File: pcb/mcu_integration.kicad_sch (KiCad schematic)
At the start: 28 parts, among them J1 Micro_SD_Card, U1 STM32F103RBTx, Y1 ECS-80-18-5PX-GM-TR

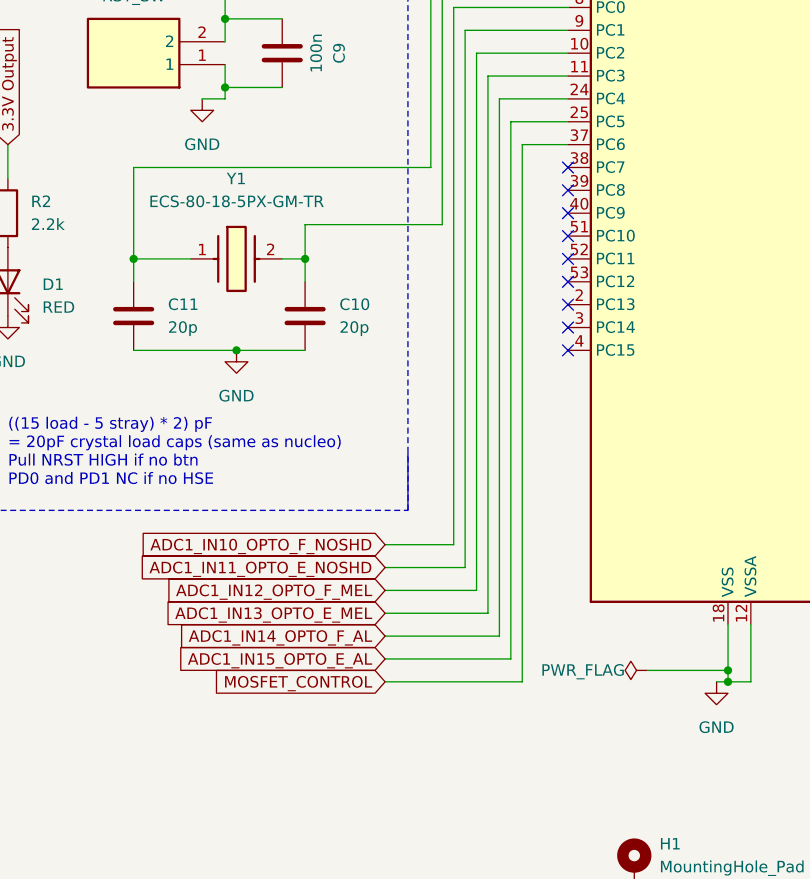
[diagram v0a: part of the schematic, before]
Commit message: mcu square wave sine header, more space for ic's should be ready for order
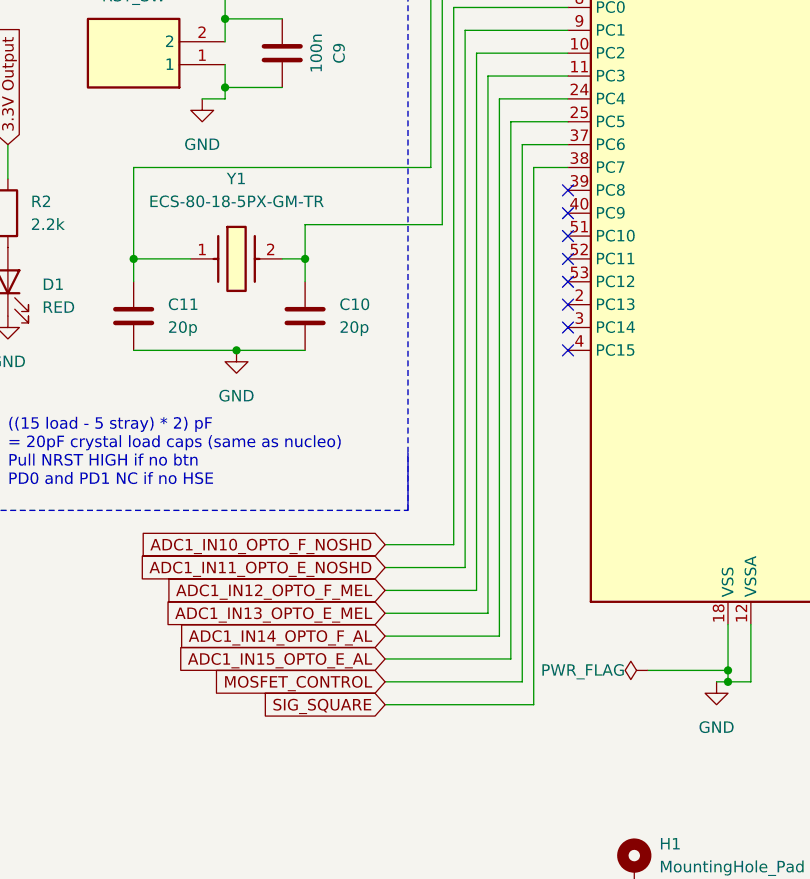
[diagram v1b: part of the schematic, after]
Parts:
- C1: footprint Capacitor_SMD:C_0402_1005Metric -> Resistor_SMD:R_0402_1005Metric
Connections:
- net SIG_SQUARE: now reaches U1.38 (PC7)
- no-connect marks 27 -> 26
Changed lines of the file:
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@@
   (no_connect (at 116.84 107.95))
   (no_connect (at 81.28 85.09))
-  (no_connect (at 81.28 74.93))
   (no_connect (at 81.28 80.01))
   (no_connect (at 116.84 90.17))
@@
     (stroke (width 0) (type default))
   )
+  (wire (pts (xy 60.96 134.62) (xy 77.47 134.62))
+    (stroke (width 0) (type default))
+  )
   (polyline (pts (xy 13.97 113.03) (xy 63.5 113.03))
     (stroke (width 0) (type dash))
@@
     (stroke (width 0) (type default))
   )
+  (wire (pts (xy 77.47 134.62) (xy 77.47 74.93))
+    (stroke (width 0) (type default))
+  )
   (wire (pts (xy 116.84 39.37) (xy 127 39.37))
     (stroke (width 0) (type default))
@@
   )
   (wire (pts (xy 71.12 121.92) (xy 71.12 62.23))
+    (stroke (width 0) (type default))
+  )
+  (wire (pts (xy 77.47 74.93) (xy 81.28 74.93))
     (stroke (width 0) (type default))
   )
@@
     (property "Intersheetrefs" "${INTERSHEET_REFS}" (at 151.9381 46.99 0)
       (effects (font (size 1.27 1.27)) (justify left) hide)
+    )
+  )
+  (global_label "SIG_SQUARE" (shape input) (at 60.96 134.62 180) (fields_autoplaced)
+    (effects (font (size 1.27 1.27)) (justify right))
+    (property "Intersheetrefs" "${INTERSHEET_REFS}" (at 46.5448 134.62 0)
+      (effects (font (size 1.27 1.27)) (justify right) hide)
     )
   )
@@
       (effects (font (size 1.27 1.27)) (justify left))
     )
-    (property "Footprint" "Capacitor_SMD:C_0402_1005Metric" (at 40.3352 31.75 0)
-      (effects (font (size 1.27 1.27)) hide)
-    )
+    (property "Footprint" "Resistor_SMD:R_0402_1005Metric" (at 40.3352 31.75 0)
+      (effects (font (size 1.27 1.27)) hide)
+    )
